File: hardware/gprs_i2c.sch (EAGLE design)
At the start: 88 parts, among them IC1 SIM900, J2 U.FL, Q1 si2305cd, Q2 PMBF170, Q3 PMBF170, Q4 si2305cd, Q5 si2305cd, T1 BC846, T2 BC846, T3 BC846, T4 BC846, U1 SPX5205 3v3, U3 TC1014 2V8, X2 bat, X3 prog, X4 ts, X5 MOLEX_4HORIZONTAL, X6 MOLEX_4HORIZONTAL, Y1 32768Hz CFPX-217 12.5pF

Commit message: pcb routing stage1
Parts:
- removed C15: 100uF, rcl:C-EUC1206
- removed Q1: si2305cd, Simplex-DiscreteSemi:MOSFET-PCHANNELSMD_POWER
- removed R7: 220K, rcl:R-EU_R0805W
- removed R8: 100K, rcl:R-EU_R0805W
- removed T3: BC846, transistor:BC846
- removed X3: prog, Simplex-Connectors:MOLEX_6HORIZONTAL
- added C5: 100nF, rcl:C-EUC0805
- added G1: HU2032-LF, Simplex-Battery:HU2032-LF
- added IC2: DS3231, Simplex-ICs:DS3231
- added R1: 10k, rcl:R-EU_R0805W
- added X1: prog, Simplex-Connectors:MOLEX_6VERTICAL
- X5: value MOLEX_4HORIZONTAL -> i2c
- X6: value MOLEX_4HORIZONTAL -> pwr
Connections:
- removed net N$12: Q1.G, R7.2, T3.C
- removed net N$13: R8.2, T3.B
- removed net P4.0: U$1.29
- removed net P4.1: U$1.30
- new net N$9: IC2.32KHZ, R1.2
- net 2V8: now also X1.3; no longer X3.4
- net 2V8_SW: now also C5.1, IC2.VCC, R1.1
- net CE: now also U$1.45; no longer U$1.2
- net CHG: now also U$1.46; no longer U$1.15
- net CTS: now also U$1.18; no longer U$1.19
- net DTR: now also U$1.20; no longer U$1.17
- net GND: now also C5.2, G1.-, IC2.!RST, IC2.GND, IC2.NC@0, IC2.NC@1, IC2.NC@2, IC2.NC@3, IC2.NC@4, IC2.NC@5, IC2.NC@6, IC2.NC@7, U$17.A1, X1.6; no longer C15.2, T3.E, X3.1
- net GPRS_PWRKEY: now also U$1.29; no longer U$1.21
- net GPRS_VBAT: now also U$1.30; no longer U$1.22
- net I2C_EN: now also U1.EN; no longer R8.1
- net N$5: now also G1.+, IC2.VBAT; no longer C3.1, C6.1, Q1.D, U1.EN, U1.IN
- net RI: now also U$1.19; no longer U$1.18
- net RST: now also X1.5; no longer X3.2
- net RTS: now also U$1.17; no longer U$1.20
- net SCL_L: now also IC2.SCL
- net SDA_L: now also IC2.SDA
- net STATUS: now also U$1.2; no longer U$1.16
- net TEST: now also X1.4; no longer X3.3
- net UART_RX: now also X1.2; no longer X3.5
- net UART_TX: now also X1.1; no longer X3.6
- net VBAT: no longer C15.1
- net VIN: now also C3.1, C6.1, U1.IN; no longer Q1.S, R7.1
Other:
- moved on the sheet: C16, C20, C21, C25, U$17

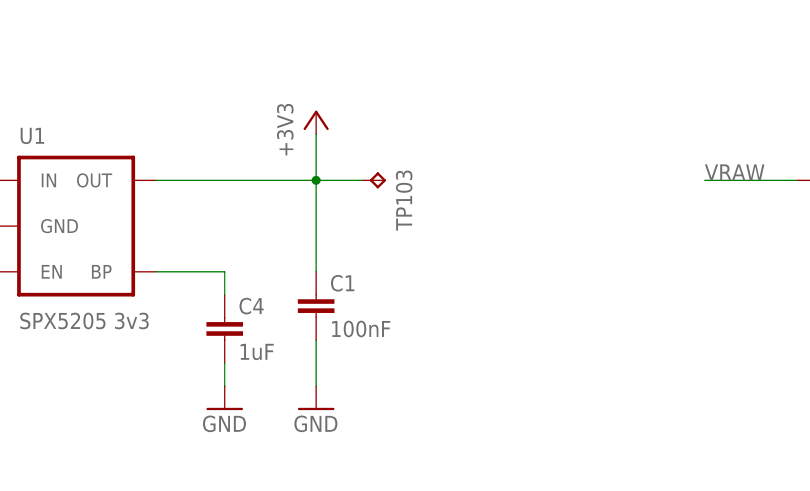
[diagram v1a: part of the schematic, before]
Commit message: pcb reouting part2
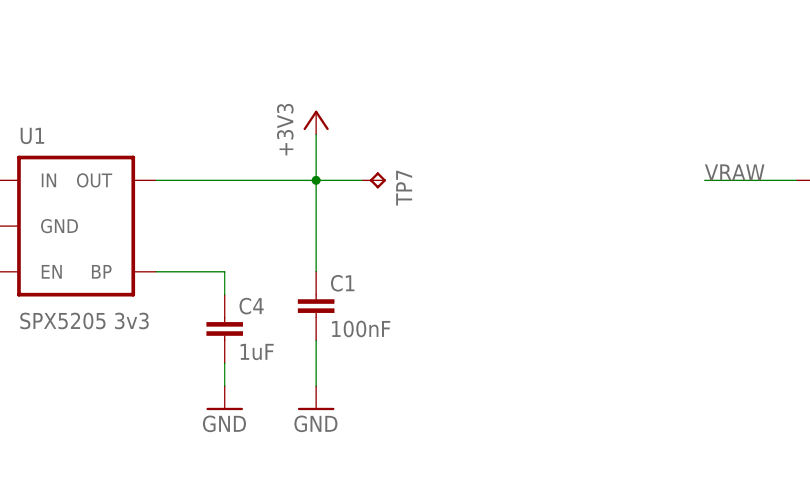
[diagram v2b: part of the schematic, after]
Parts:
- renumbered TP103 to TP7
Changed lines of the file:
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@@
 <part name="C21" library="rcl" deviceset="C-EU" device="C1206" value="100uF"/>
 <part name="GND19" library="SparkFun" deviceset="GND" device=""/>
-<part name="TP103" library="testpad" deviceset="TP" device="TP12R"/>
+<part name="TP7" library="testpad" deviceset="TP" device="TP12R"/>
 <part name="TP102" library="testpad" deviceset="TP" device="TP12R"/>
 <part name="TP1" library="testpad" deviceset="TP" device="TP12R"/>
@@
 <instance part="C21" gate="G$1" x="294.64" y="287.02"/>
 <instance part="GND19" gate="1" x="294.64" y="279.4"/>
-<instance part="TP103" gate="G$1" x="91.44" y="292.1" rot="R270"/>
+<instance part="TP7" gate="G$1" x="91.44" y="292.1" rot="R270"/>
 <instance part="TP102" gate="G$1" x="60.96" y="248.92"/>
 <instance part="TP1" gate="G$1" x="17.78" y="185.42"/>
@@
 <pinref part="C1" gate="G$1" pin="1"/>
 <pinref part="+3V1" gate="G$1" pin="+3V3"/>
-<pinref part="TP103" gate="G$1" pin="TP"/>
+<pinref part="TP7" gate="G$1" pin="TP"/>
 <wire x1="83.82" y1="292.1" x2="88.9" y2="292.1" width="0.1524" layer="91"/>
 </segment>
